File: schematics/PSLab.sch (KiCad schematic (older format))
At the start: 78 parts, among them J1 Programmer, J10 GND, J11 Vbus, J13 D+, J14 D-, J15 External Power, J16 I2C-2, J2 DoublePins, J5 Bluetooth, J6 I2C-1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

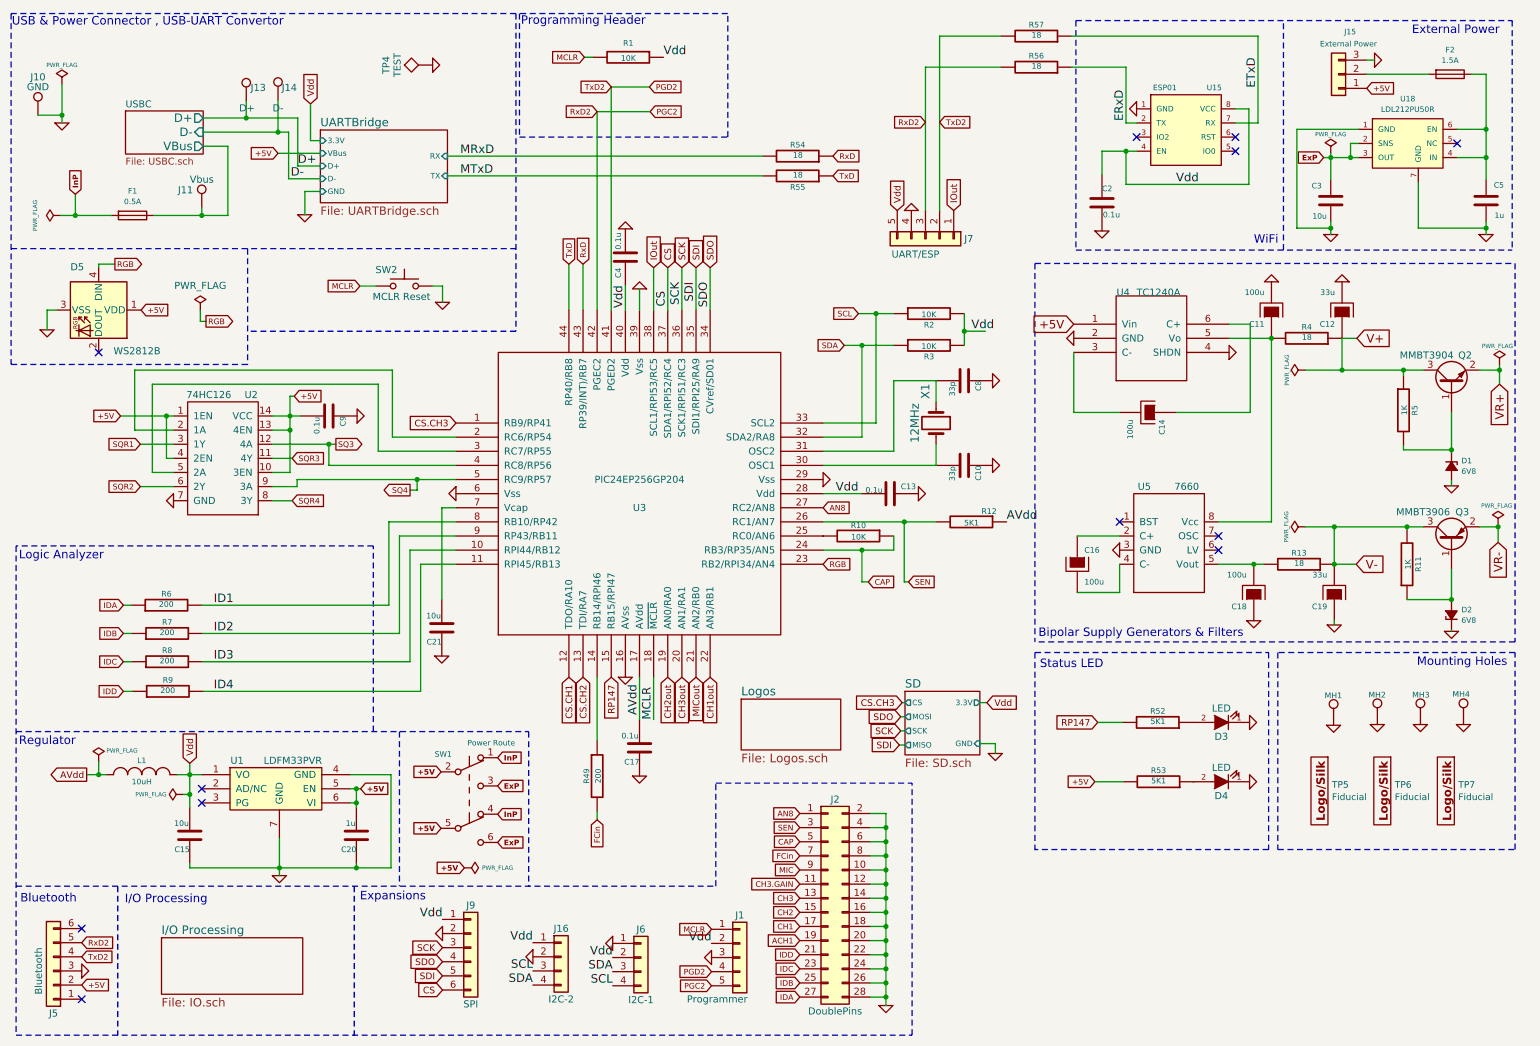
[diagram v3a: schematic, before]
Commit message: refactor: fixed rotation in resistors
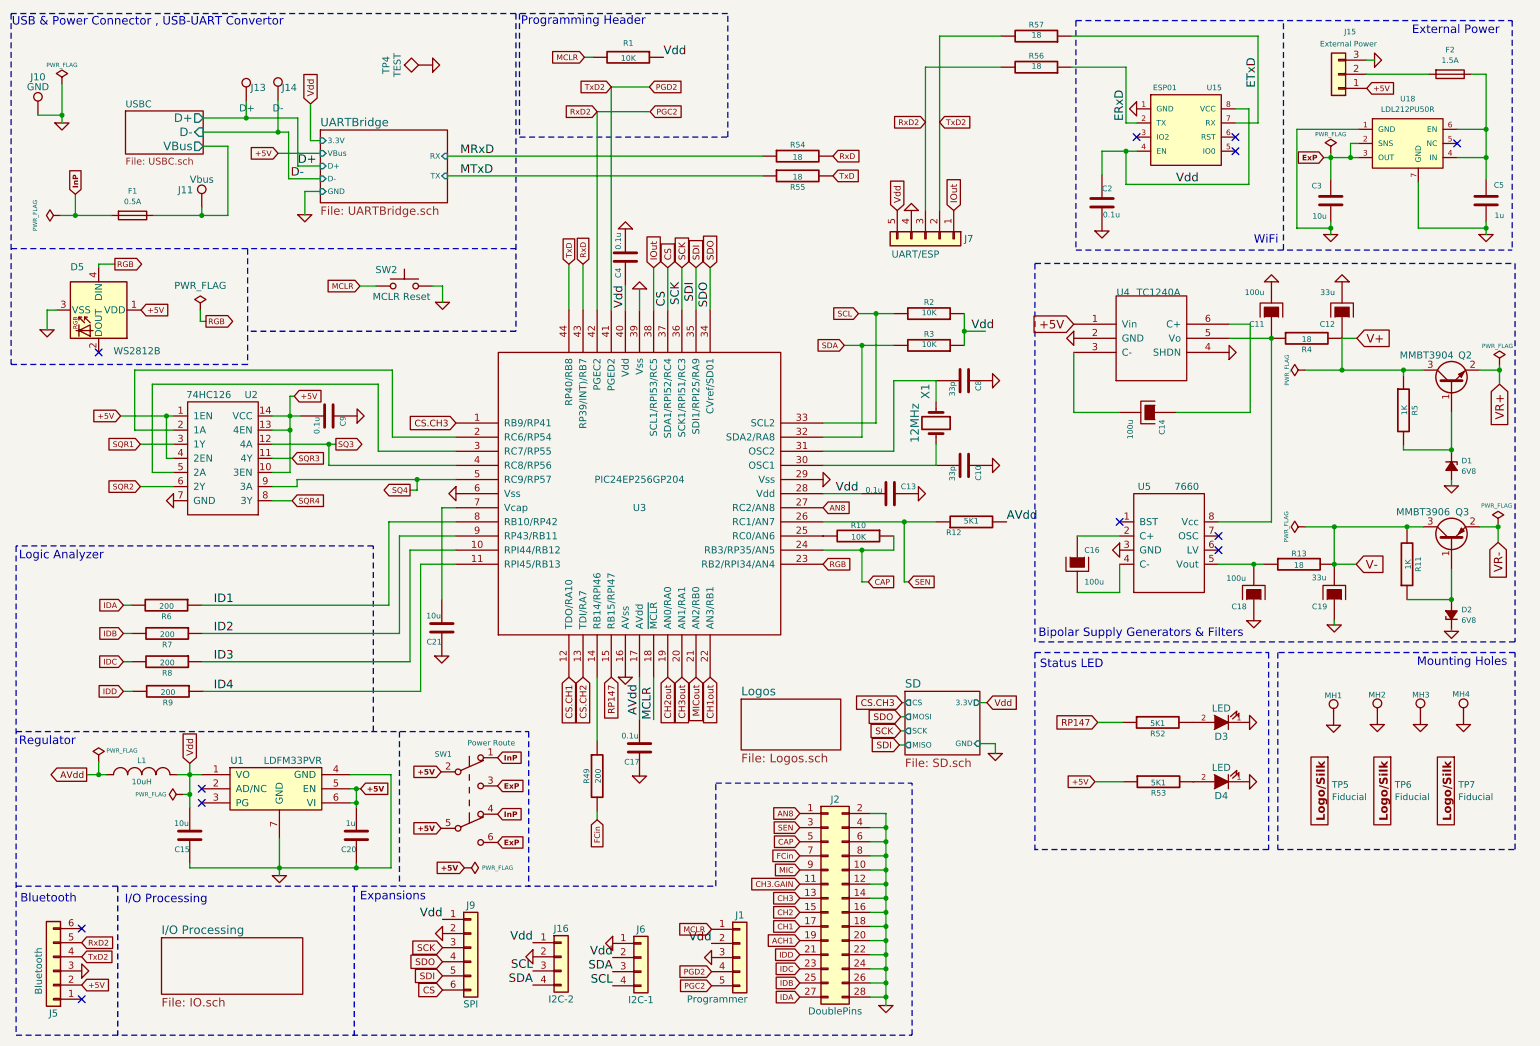
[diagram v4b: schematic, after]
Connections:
- net +5V: now also R53.1; no longer R53.2
- net AVdd: now also R12.2; no longer R12.1
- net ID1: now also R6.1; no longer R6.2
- net ID2: now also R7.1; no longer R7.2
- net ID3: now also R8.1; no longer R8.2
- net ID4: now also R9.1; no longer R9.2
- net IDA: now also R6.2; no longer R6.1
- net IDB: now also R7.2; no longer R7.1
- net IDC: now also R8.2; no longer R8.1
- net IDD: now also R9.2; no longer R9.1
- net MRxD: now also R54.1; no longer R54.2
- net MTxD: now also R55.1; no longer R55.2
- net RP147: now also R52.1; no longer R52.2
- net RxD: now also R54.2; no longer R54.1
- net SCL: now also R2.2; no longer R2.1
- net SDA: now also R3.2; no longer R3.1
- net SEN: now also R12.1; no longer R12.2
- net TxD: now also R55.2; no longer R55.1
- net V+: now also R4.2; no longer R4.1
- net V-: now also R13.2; no longer R13.1
- net Vdd: now also R2.1, R3.1; no longer R2.2, R3.2
- net at C11.1, U4.5 (Vo), U5.8 (Vcc): now also R4.1; no longer R4.2
- net at C18.2, U5.5 (Vout): now also R13.1; no longer R13.2
- net at D3.2 (A): now also R52.2; no longer R52.1
- net at D4.2 (A): now also R53.2; no longer R53.1
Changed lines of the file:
@@
 F 3 "" H 1605 4890 30  0000 C CNN
 	1    1605 4890
-	0    -1   -1   0
+	0    1    1    0
 $EndComp
 $Comp
@@
 F 3 "" H 1600 4690 30  0000 C CNN
 	1    1600 4690
-	0    -1   -1   0
+	0    1    1    0
 $EndComp
 $Comp
@@
 F 3 "" H 7000 2850 30  0000 C CNN
 	1    7000 2850
-	0    -1   1    0
-$EndComp
-$Comp
-L PSLab-rescue:R-RESCUE-proto1 R2
-U 1 1 5421BED8
-P 7000 2625
-F 0 "R2" V 7080 2625 40  0000 C CNN
-F 1 "10K" V 7007 2626 40  0000 C CNN
-F 2 "Resistor_SMD:R_0603_1608Metric" V 6930 2625 30  0001 C CNN
-F 3 "" H 7000 2625 30  0000 C CNN
-	1    7000 2625
-	0    -1   1    0
+	0    1    -1   0
 $EndComp
 Text Label 3680 1650 0    60   ~ 0
@@
 F 3 "" H 1605 5090 30  0000 C CNN
 	1    1605 5090
-	0    -1   -1   0
+	0    1    1    0
 $EndComp
 $Comp
@@
 F 3 "" H 1610 5300 30  0000 C CNN
 	1    1610 5300
-	0    -1   -1   0
+	0    1    1    0
 $EndComp
 $Comp
@@
 P 9300 4600
 F 0 "C18" H 9350 4700 40  0000 L CNN
-F 1 "100u" H 9350 4475 40  0000 L CNN
+F 1 "100u" H 9355 4500 40  0000 L CNN
 F 2 "Capacitors_Tantalum_SMD:CP_Tantalum_Case-C_EIA-6032-28_Reflow" H 9400 4450 30  0001 C CNN
 F 3 "" H 9300 4600 300 0000 C CNN
@@
 F 3 "" H 9675 2800 30  0000 C CNN
 	1    9675 2800
-	0    1    -1   0
+	0    -1   1    0
 $EndComp
 $Comp
@@
 U 1 1 5565746E
 P 9620 4400
-F 0 "R13" V 9700 4400 40  0000 C CNN
+F 0 "R13" V 9545 4400 40  0000 C CNN
 F 1 "18" V 9627 4401 40  0000 C CNN
 F 2 "Resistor_SMD:R_0603_1608Metric" V 9550 4400 30  0001 C CNN
 F 3 "" H 9620 4400 30  0000 C CNN
 	1    9620 4400
-	0    1    -1   0
+	0    -1   1    0
 $EndComp
 $Comp
@@
 P 9870 4600
 F 0 "C19" H 9920 4700 40  0000 L CNN
-F 1 "33u" H 9920 4475 40  0000 L CNN
+F 1 "33u" H 9925 4495 40  0000 L CNN
 F 2 "Capacitors_Tantalum_SMD:CP_Tantalum_Case-B_EIA-3528-21_Reflow" H 9970 4450 30  0001 C CNN
 F 3 "" H 9870 4600 300 0000 C CNN
@@
 F 3 "" H 7300 4100 30  0000 C CNN
 	1    7300 4100
-	0    1    1    0
+	0    -1   -1   0
 $EndComp
 Text Label 9330 1025 1    60   ~ 0
@@
 F 3 "" H 8620 5520 30  0000 C CNN
 	1    8620 5520
-	0    1    -1   0
+	0    -1   1    0
 $EndComp
 $Comp
@@
 F 3 "" H 8625 5940 30  0000 C CNN
 	1    8625 5940
-	0    1    -1   0
+	0    -1   1    0
 $EndComp
 $Comp
@@
 U 1 1 566549A7
 P 6070 1650
-F 0 "R55" V 5990 1650 40  0000 C CNN
+F 0 "R55" V 6150 1650 40  0000 C CNN
 F 1 "18" V 6077 1651 40  0000 C CNN
 F 2 "Resistor_SMD:R_0603_1608Metric" V 6000 1650 30  0001 C CNN
 F 3 "" H 6070 1650 30  0000 C CNN
 	1    6070 1650
-	0    1    -1   0
+	0    -1   1    0
 $EndComp
 $Comp
@@
 U 1 1 56655363
 P 6070 1510
-F 0 "R54" V 6150 1510 40  0000 C CNN
+F 0 "R54" V 5990 1510 40  0000 C CNN
 F 1 "18" V 6077 1511 40  0000 C CNN
 F 2 "Resistor_SMD:R_0603_1608Metric" V 6000 1510 30  0001 C CNN
 F 3 "" H 6070 1510 30  0000 C CNN
 	1    6070 1510
-	0    1    -1   0
+	0    -1   1    0
 $EndComp
 Wire Wire Line
@@
 Wire Wire Line
 	1840 2680 1880 2680
+$Comp
+L PSLab-rescue:R-RESCUE-proto1 R2
+U 1 1 5421BED8
+P 7000 2625
+F 0 "R2" V 7080 2625 40  0000 C CNN
+F 1 "10K" V 7007 2626 40  0000 C CNN
+F 2 "Resistor_SMD:R_0603_1608Metric" V 6930 2625 30  0001 C CNN
+F 3 "" H 7000 2625 30  0000 C CNN
+	1    7000 2625
+	0    1    -1   0
+$EndComp
 $EndSCHEMATC

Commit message: docs: updated pos and bom files
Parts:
- U1: value LDFM33PVR -> LDFM33PUR; symbol PSLab:LDFM33PVR -> PSLab:LDFM33PUR
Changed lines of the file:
@@
 $EndComp
 $Comp
-L PSLab:LDFM33PVR U1
+L PSLab:LDFM33PUR U1
 U 1 1 5C57C10F
 P 2400 5990
 F 0 "U1" H 2100 6190 50  0000 C CNN
-F 1 "LDFM33PVR" H 2495 6190 50  0000 C CNN
+F 1 "LDFM33PUR" H 2495 6190 50  0000 C CNN
 F 2 "Housings_DFN_QFN:DFN-6-1EP_3x3mm_Pitch0.95mm" H 2400 5990 60  0001 C CNN
 F 3 "https://www.mouser.com/datasheet/2/389/ldfm-974225.pdf" H 2400 5990 60  0001 C CNN

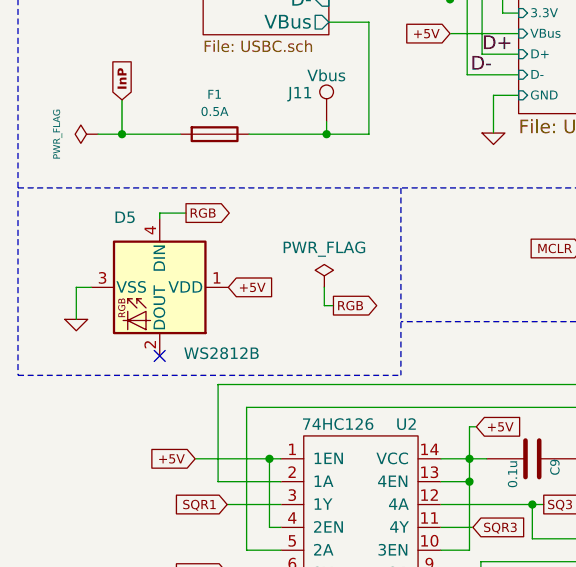
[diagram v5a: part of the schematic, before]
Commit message: fix: courtyars, F2 fuse and RGB LED diode
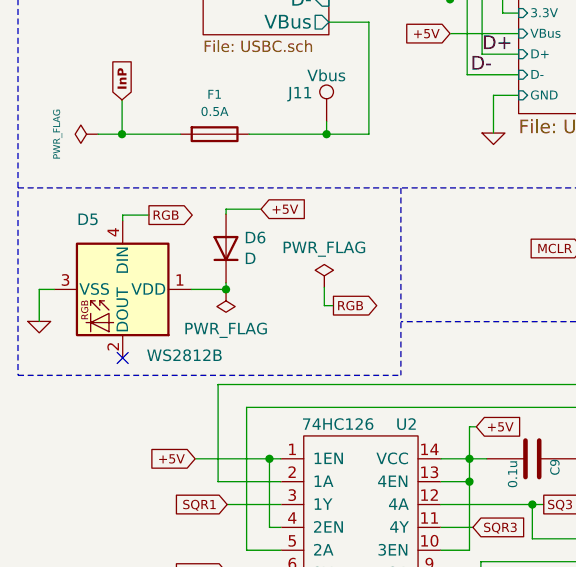
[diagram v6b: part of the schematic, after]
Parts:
- added D6: D, Diode_SMD:D_MiniMELF, symbol Device:D
- F2: footprint Fuse:Fuse_1812_4532Metric -> Fuse:Fuse_1206_3216Metric
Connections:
- net +5V: now also D6.2 (A); no longer D5.1 (VDD)
- new net: D5.1 (VDD), D6.1 (K)
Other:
- moved on the sheet: D5
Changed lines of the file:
@@
 F 0 "F2" V 10517 930 39  0000 C CNN
 F 1 "1.5A" V 10592 930 39  0000 C CNN
-F 2 "Fuse:Fuse_1812_4532Metric" V 10620 930 50  0001 C CNN
+F 2 "Fuse:Fuse_1206_3216Metric" V 10620 930 50  0001 C CNN
 F 3 "https://www.mouser.fi/datasheet/2/240/Littelfuse_PTC_1812L_Datasheet.pdf-693388.pdf" H 10690 930 50  0001 C CNN
 	1    10690 930
@@
 L LED:WS2812B D5
 U 1 1 5F65D829
-P 1120 2600
-F 0 "D5" V 815 2400 50  0000 L CNN
-F 1 "WS2812B" V 1410 2705 50  0000 L CNN
-F 2 "LED_SMD:LED_WS2812B_PLCC4_5.0x5.0mm_P3.2mm" H 1170 2300 50  0001 L TNN
-F 3 "https://cdn-shop.adafruit.com/datasheets/WS2812B.pdf" H 1220 2225 50  0001 L TNN
-	1    1120 2600
+P 958 2609
+F 0 "D5" V 653 2409 50  0000 L CNN
+F 1 "WS2812B" V 1248 2714 50  0000 L CNN
+F 2 "LED_SMD:LED_WS2812B_PLCC4_5.0x5.0mm_P3.2mm" H 1008 2309 50  0001 L TNN
+F 3 "https://cdn-shop.adafruit.com/datasheets/WS2812B.pdf" H 1058 2234 50  0001 L TNN
+	1    958  2609
 	0    1    1    0
 $EndComp
@@
 L PSLab-rescue:GND-RESCUE-proto1 #PWR033
 U 1 1 5F6AB933
-P 755 2740
-F 0 "#PWR033" H 755 2740 30  0001 C CNN
-F 1 "GND" H 755 2670 30  0001 C CNN
-F 2 "" H 755 2740 60  0000 C CNN
-F 3 "" H 755 2740 60  0000 C CNN
-	1    755  2740
-	1    0    0    -1
-$EndComp
-Wire Wire Line
-	755  2740 755  2600
-Wire Wire Line
-	755  2600 820  2600
-NoConn ~ 1120 2900
-Text GLabel 1420 2600 2    40   Input ~ 0
-+5V
-Wire Wire Line
-	1120 2275 1120 2300
-Wire Wire Line
-	1235 2275 1120 2275
+P 593 2749
+F 0 "#PWR033" H 593 2749 30  0001 C CNN
+F 1 "GND" H 593 2679 30  0001 C CNN
+F 2 "" H 593 2749 60  0000 C CNN
+F 3 "" H 593 2749 60  0000 C CNN
+	1    593  2749
+	1    0    0    -1
+$EndComp
+Wire Wire Line
+	593  2749 593  2609
+Wire Wire Line
+	593  2609 658  2609
+NoConn ~ 958  2909
+Text GLabel 1563 2258 2    40   Input ~ 0
++5V
+Wire Wire Line
+	958  2284 958  2309
+Wire Wire Line
+	1073 2284 958  2284
 Text GLabel 6250 4400 2    40   Input ~ 0
 RGB
-Text GLabel 1235 2275 2    40   Output ~ 0
+Text GLabel 1073 2284 2    40   Output ~ 0
 RGB
 $Comp
@@
 	0    1    -1   0
 $EndComp
+$Comp
+L Device:D D6
+U 1 1 5F978449
+P 1410 2430
+F 0 "D6" V 1456 2350 50  0000 R CNN
+F 1 "D" V 1365 2350 50  0000 R CNN
+F 2 "Diode_SMD:D_MiniMELF" H 1410 2430 50  0001 C CNN
+F 3 "~" H 1410 2430 50  0001 C CNN
+	1    1410 2430
+	0    -1   -1   0
+$EndComp
+Wire Wire Line
+	1258 2609 1410 2609
+Wire Wire Line
+	1410 2609 1410 2580
+Wire Wire Line
+	1410 2280 1410 2258
+Wire Wire Line
+	1410 2258 1563 2258
+$Comp
+L power:PWR_FLAG #FLG0106
+U 1 1 5FA4B8DD
+P 1410 2609
+F 0 "#FLG0106" H 1410 2684 50  0001 C CNN
+F 1 "PWR_FLAG" H 1410 2782 50  0000 C CNN
+F 2 "" H 1410 2609 50  0001 C CNN
+F 3 "~" H 1410 2609 50  0001 C CNN
+	1    1410 2609
+	-1   0    0    1
+$EndComp
+Connection ~ 1410 2609
 $EndSCHEMATC
